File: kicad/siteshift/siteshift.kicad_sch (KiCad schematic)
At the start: 47 parts, among them SW1 Reset, U1 DRV8873HPWPRQ1, U2 Pico, U3 L7805, U4 ULN2004A

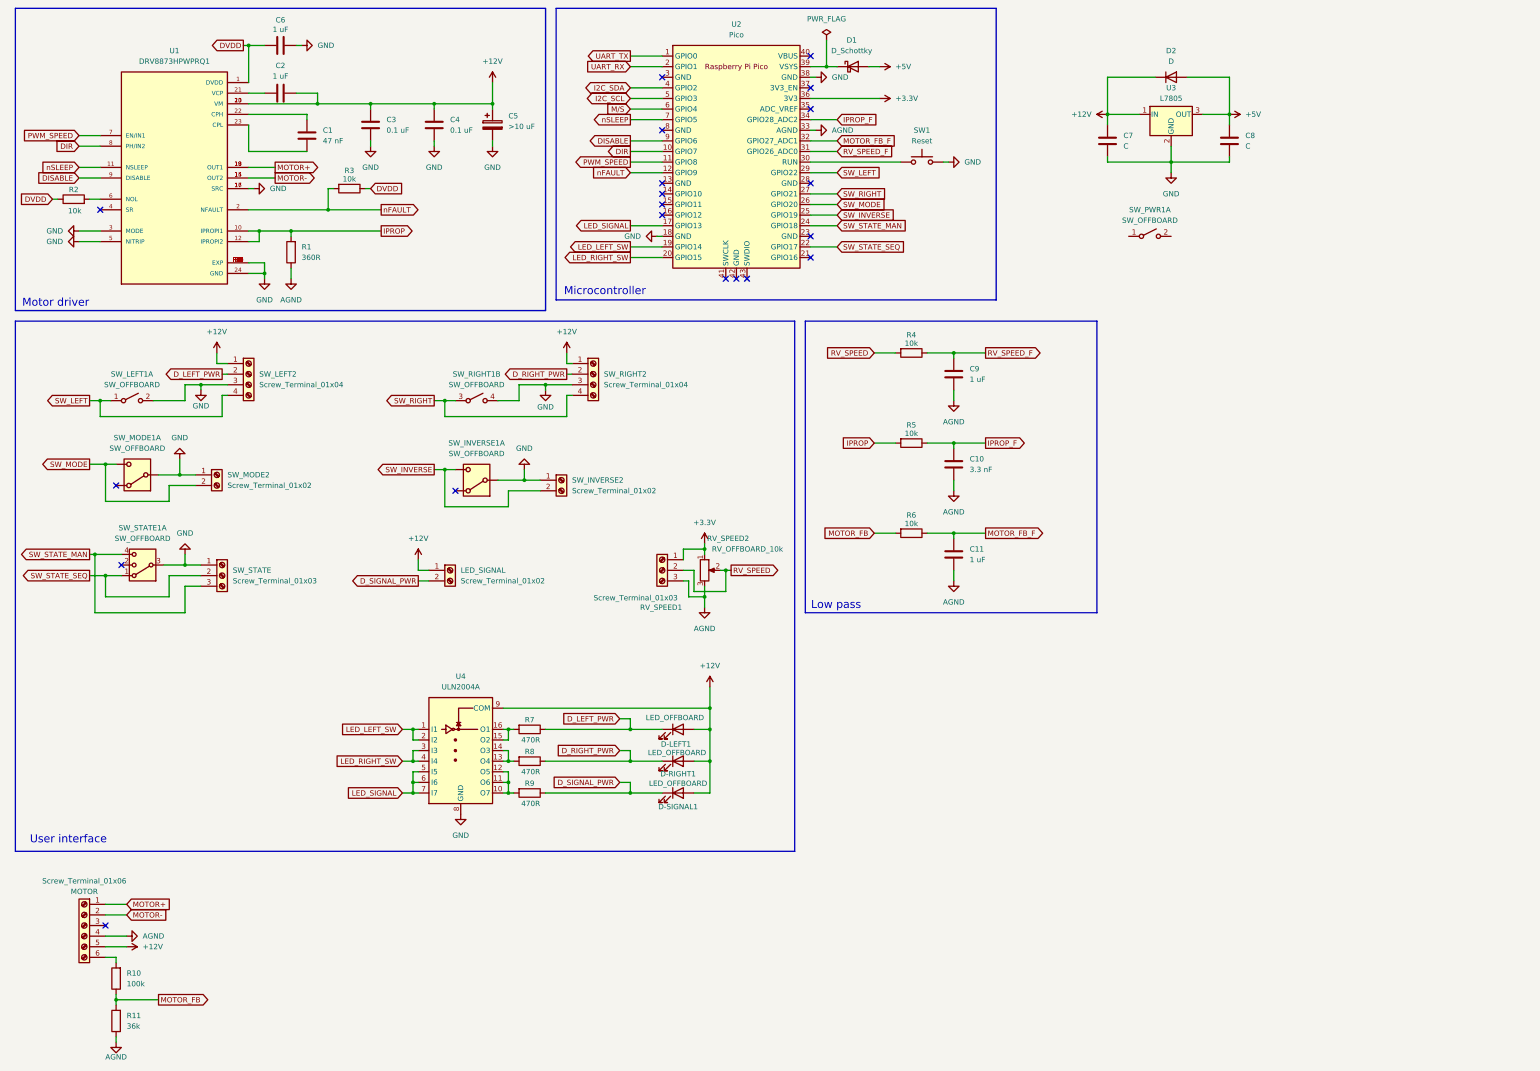
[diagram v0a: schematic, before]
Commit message: Wire power distribution
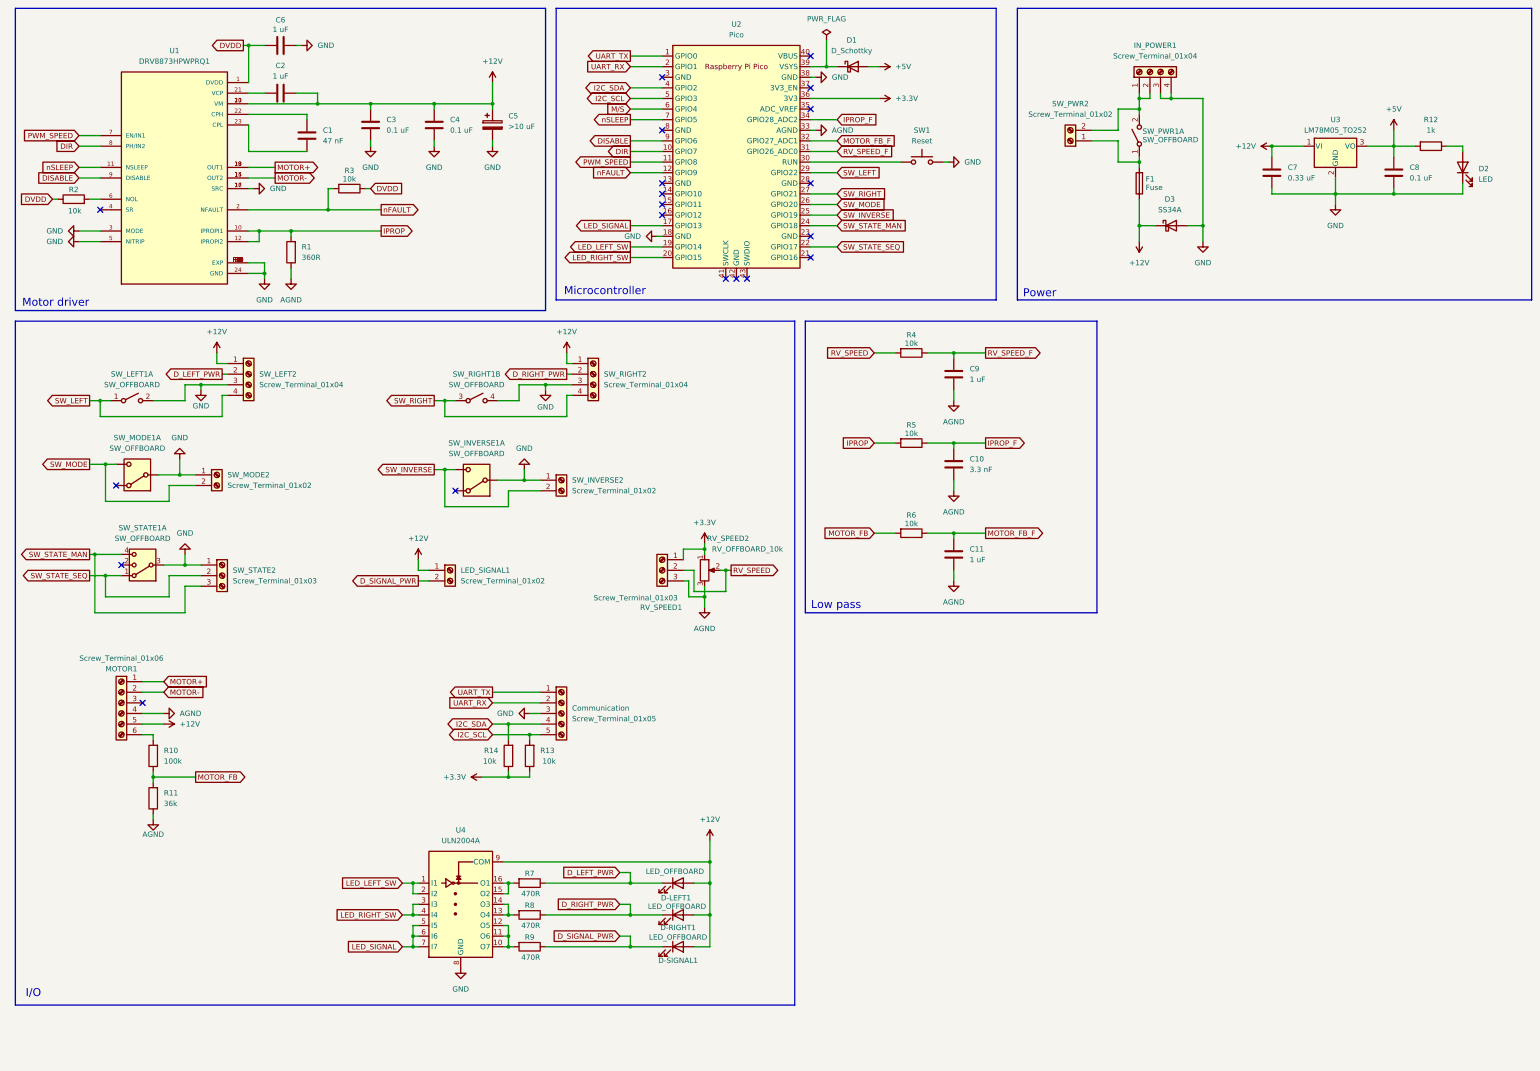
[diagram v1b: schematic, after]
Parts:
- removed D2: D, Diode_SMD:D_1206_3216Metric_Pad1.42x1.75mm_HandSolder, symbol Device:D
- removed U3: L7805, Package_TO_SOT_THT:TO-220-3_Vertical, symbol Regulator_Linear:L7805
- added Communication: Screw_Terminal_01x05, symbol Connector:Screw_Terminal_01x05
- added D2: LED, Diode_SMD:D_1206_3216Metric_Pad1.42x1.75mm_HandSolder, symbol Device:LED
- added D3: SS34A, Diode_SMD:D_SMA_Handsoldering, symbol Device:D_Schottky
- added F1: Fuse, symbol Device:Fuse
- added IN_POWER1: Screw_Terminal_01x04, symbol Connector:Screw_Terminal_01x04
- added R12: 1k, Resistor_SMD:R_1206_3216Metric_Pad1.30x1.75mm_HandSolder, symbol Device:R
- added R13, R14: 10k, symbol Device:R
- added SW_PWR2: Screw_Terminal_01x02, symbol Connector:Screw_Terminal_01x02
- added U3: LM78M05_TO252, Package_TO_SOT_SMD:TO-252-2, symbol Regulator_Linear:LM78M05_TO252
- C7: value C -> 0.33 uF
- C8: value C -> 0.1 uF
- renumbered LED_SIGNAL to LED_SIGNAL1, MOTOR to MOTOR1, SW_STATE to SW_STATE2
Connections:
- net +12V: now also D3.1 (K), F1.1, U3.1 (VI)
- net +3.3V: now also R13.1, R14.1
- net +5V: now also R12.2, U3.3 (VO)
- net GND: now also Communication.3 (Pin_3), D2.1 (K), D3.2 (A), IN_POWER1.3 (Pin_3), IN_POWER1.4 (Pin_4), U3.2 (GND)
- net I2C_SCL: now also Communication.5 (Pin_5), R13.2
- net I2C_SDA: now also Communication.4 (Pin_4), R14.2
- net UART_RX: now also Communication.2 (Pin_2)
- net UART_TX: now also Communication.1 (Pin_1)
- net at SW_PWR1.1 (A): now also F1.2, SW_PWR2.1 (Pin_1)
- net at SW_PWR1.2 (B): now also IN_POWER1.1 (Pin_1), IN_POWER1.2 (Pin_2), SW_PWR2.2 (Pin_2)
- new net: D2.2 (A), R12.1
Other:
- note added: "I/O"
- note added: "Power"
- note removed: "User interface"
- moved on the sheet: C7, C8, D-LEFT1, D-RIGHT1, D-SIGNAL1, MOTOR1, R10, R11, R7, R8, R9, SW_PWR1A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

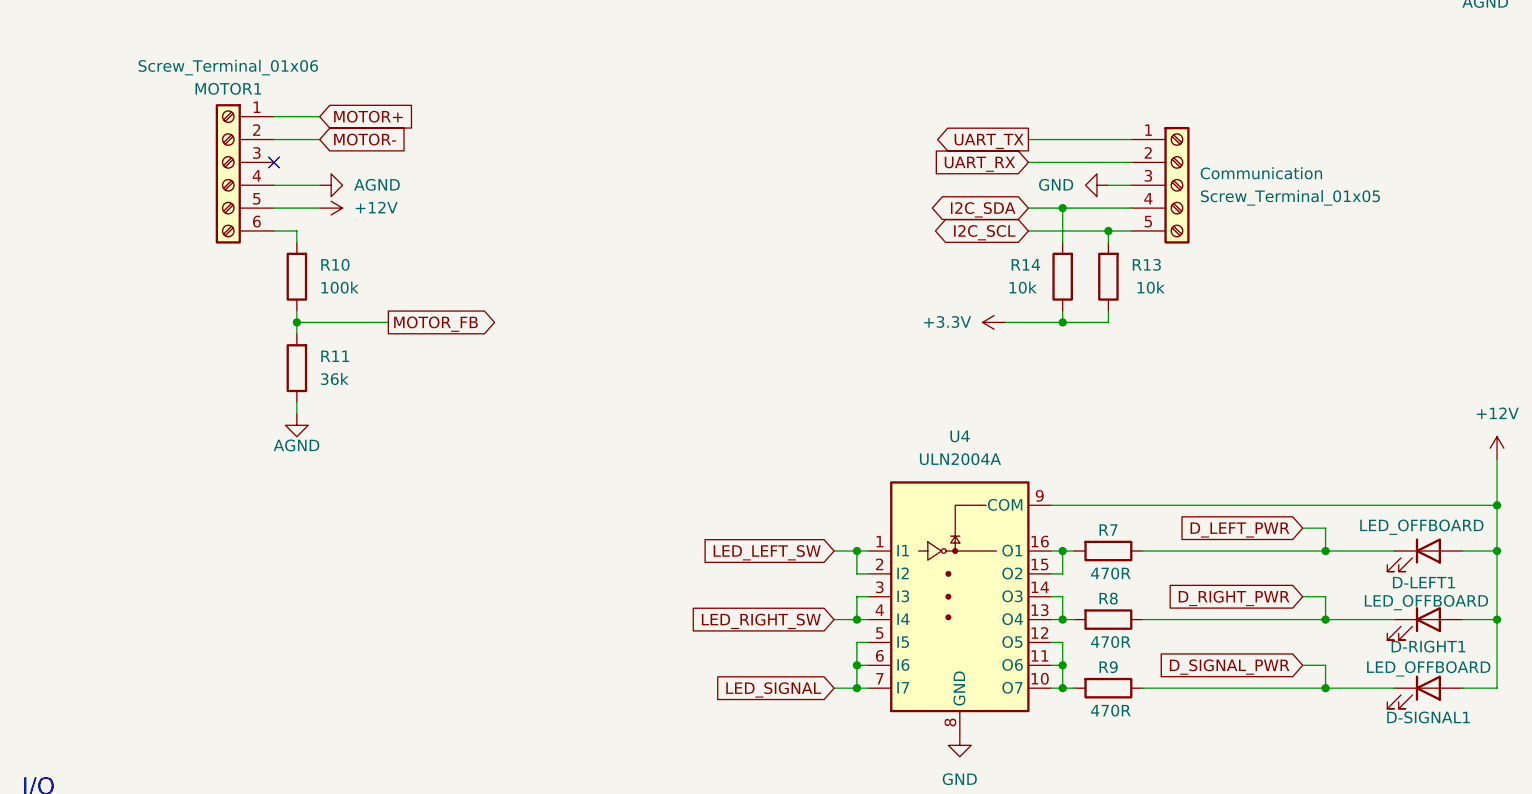
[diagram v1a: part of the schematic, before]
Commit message: Assign footprints
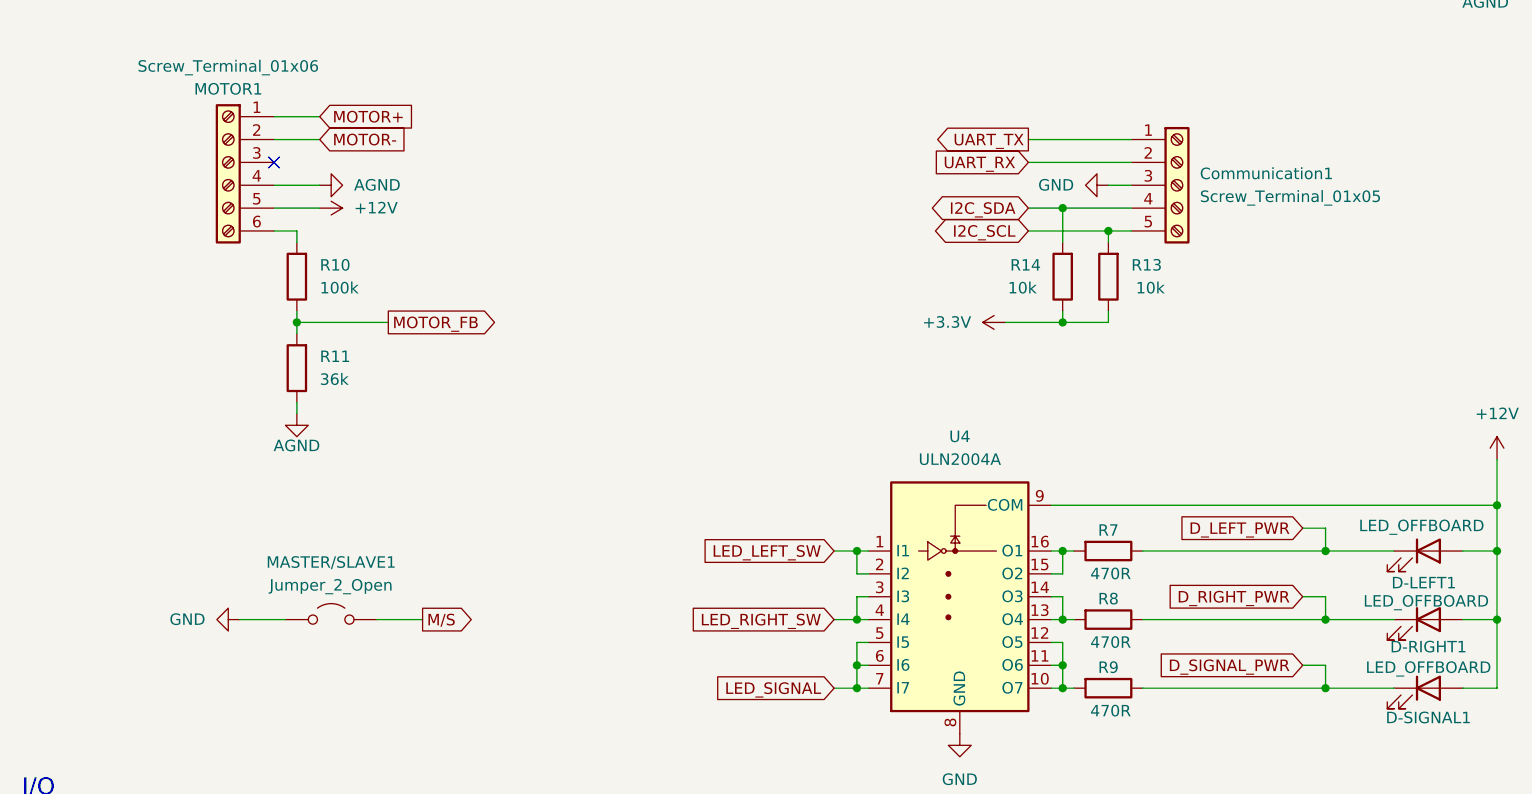
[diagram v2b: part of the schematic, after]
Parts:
- added MASTER/SLAVE1: Jumper_2_Open, Connector_PinHeader_2.54mm:PinHeader_1x03_P2.54mm_Vertical, symbol Jumper:Jumper_2_Open
- C1, C10, C11, C2, C3, C4, C6, C9: footprint (none) -> Capacitor_SMD:C_1206_3216Metric_Pad1.33x1.80mm_HandSolder
- C5: footprint (none) -> Capacitor_Tantalum_SMD:CP_EIA-6032-20_AVX-F_Pad2.25x2.35mm_HandSolder
- Communication1: renamed from Communication; footprint (none) -> TerminalBlock_MetzConnect:TerminalBlock_MetzConnect_Type101_RT01605HBWC_1x05_P5.08mm_Horizontal
- D3: footprint Diode_SMD:D_SMA_Handsoldering -> Diode_SMD:D_SMB-SMC_Universal_Handsoldering
- F1: footprint (none) -> Fuse:Fuse_Blade_ATO_directSolder
- IN_POWER1, SW_LEFT2, SW_RIGHT2: footprint (none) -> TerminalBlock_MetzConnect:TerminalBlock_MetzConnect_Type101_RT01604HBWC_1x04_P5.08mm_Horizontal
- LED_SIGNAL1, SW_INVERSE2, SW_MODE2, SW_PWR2: footprint (none) -> TerminalBlock_MetzConnect:TerminalBlock_MetzConnect_Type101_RT01602HBWC_1x02_P5.08mm_Horizontal
- MOTOR1: footprint (none) -> TerminalBlock_MetzConnect:TerminalBlock_MetzConnect_Type101_RT01606HBWC_1x06_P5.08mm_Horizontal
- R1, R10, R11, R13, R14, R2, R3, R4, R5, R6, R7, R8, R9: footprint (none) -> Resistor_SMD:R_1206_3216Metric_Pad1.30x1.75mm_HandSolder
- RV_SPEED1, SW_STATE2: footprint (none) -> TerminalBlock_MetzConnect:TerminalBlock_MetzConnect_Type101_RT01603HBWC_1x03_P5.08mm_Horizontal
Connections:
- net GND: now also MASTER/SLAVE1.1 (A)
- net M/S: now also MASTER/SLAVE1.2 (B)

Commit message: first pcb design
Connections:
- net GND: now also U2.3 (GND); no longer U2.18 (GND)

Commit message: PCB design update
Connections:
- net IPROP_F: now also U2.31 (GPIO26_ADC0); no longer U2.34 (GPIO28_ADC2)
- net RV_SPEED_F: now also U2.34 (GPIO28_ADC2); no longer U2.31 (GPIO26_ADC0)
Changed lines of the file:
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@@
+		)
+	)
+	(global_label "RV_SPEED_F"
+		(shape input)
+		(at 210.82 40.64 0)
+		(fields_autoplaced yes)
+		(effects
+			(font
+				(size 1.27 1.27)
+			)
+			(justify left)
+		)
+		(property "Intersheetrefs" "${INTERSHEET_REFS}"
+			(at 225.2351 40.64 0)
+			(effects
+				(font
+					(size 1.27 1.27)
+				)
+				(justify left)
+				(hide yes)
+			)
 		)
 	)
@@
 		)
 	)
+	(global_label "PWM_SPEED"
+		(shape output)
+		(at 161.29 50.8 180)
+		(fields_autoplaced yes)
+		(effects
+			(font
+				(size 1.27 1.27)
+			)
+			(justify right)
+		)
+		(property "Intersheetrefs" "${INTERSHEET_REFS}"
+			(at 147.1169 50.8 0)
+			(effects
+				(font
+					(size 1.27 1.27)
+				)
+				(justify right)
+				(hide yes)
+			)
+		)
+	)
+	(global_label "LED_RIGHT_SW"
+		(shape output)
+		(at 161.29 73.66 180)
+		(fields_autoplaced yes)
+		(effects
+			(font
+				(size 1.27 1.27)
+			)
+			(justify right)
+		)
+		(property "Intersheetrefs" "${INTERSHEET_REFS}"
+			(at 144.8187 73.66 0)
+			(effects
+				(font
+					(size 1.27 1.27)
+				)
+				(justify right)
+				(hide yes)
+			)
+		)
+	)
+	(global_label "MOTOR_FB"
+		(shape output)
+		(at 57.15 198.12 0)
+		(fields_autoplaced yes)
+		(effects
+			(font
+				(size 1.27 1.27)
+			)
+			(justify left)
+		)
+		(property "Intersheetrefs" "${INTERSHEET_REFS}"
+			(at 69.8114 198.12 0)
+			(effects
+				(font
+					(size 1.27 1.27)
+				)
+				(justify left)
+				(hide yes)
+			)
+		)
+	)
 	(global_label "IPROP_F"
 		(shape input)
-		(at 210.82 40.64 0)
-		(fields_autoplaced yes)
-		(effects
-			(font
-				(size 1.27 1.27)
-			)
-			(justify left)
-		)
-		(property "Intersheetrefs" "${INTERSHEET_REFS}"
-			(at 221.6067 40.64 0)
+		(at 210.82 48.26 0)
+		(fields_autoplaced yes)
+		(effects
+			(font
+				(size 1.27 1.27)
+			)
+			(justify left)
+		)
+		(property "Intersheetrefs" "${INTERSHEET_REFS}"
+			(at 221.6067 48.26 0)
 			(effects
 				(font
@@
 	)
 	(global_label "PWM_SPEED"
-		(shape output)
-		(at 161.29 50.8 180)
-		(fields_autoplaced yes)
-		(effects
-			(font
-				(size 1.27 1.27)
-			)
-			(justify right)
-		)
-		(property "Intersheetrefs" "${INTERSHEET_REFS}"
-			(at 147.1169 50.8 0)
-			(effects
-				(font
-					(size 1.27 1.27)
-				)
-				(justify right)
-				(hide yes)
-			)
-		)
-	)
-	(global_label "LED_RIGHT_SW"
-		(shape output)
-		(at 161.29 73.66 180)
-		(fields_autoplaced yes)
-		(effects
-			(font
-				(size 1.27 1.27)
-			)
-			(justify right)
-		)
-		(property "Intersheetrefs" "${INTERSHEET_REFS}"
-			(at 144.8187 73.66 0)
-			(effects
-				(font
-					(size 1.27 1.27)
-				)
-				(justify right)
-				(hide yes)
-			)
-		)
-	)
-	(global_label "MOTOR_FB"
-		(shape output)
-		(at 57.15 198.12 0)
-		(fields_autoplaced yes)
-		(effects
-			(font
-				(size 1.27 1.27)
-			)
-			(justify left)
-		)
-		(property "Intersheetrefs" "${INTERSHEET_REFS}"
-			(at 69.8114 198.12 0)
-			(effects
-				(font
-					(size 1.27 1.27)
-				)
-				(justify left)
-				(hide yes)
-			)
-		)
-	)
-	(global_label "PWM_SPEED"
 		(shape input)
 		(at 29.21 44.45 180)
@@
 				(hide yes)
 			)
-		)
-	)
-	(global_label "RV_SPEED_F"
-		(shape input)
-		(at 210.82 48.26 0)
-		(fields_autoplaced yes)
-		(effects
-			(font
-				(size 1.27 1.27)
-			)
-			(justify left)
-		)
-		(property "Intersheetrefs" "${INTERSHEET_REFS}"
-			(at 225.2351 48.26 0)
-			(effects
-				(font
-					(size 1.27 1.27)
-				)
-				(justify left)
-				(hide yes)
-			)

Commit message: First code setup
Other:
- moved on the sheet: C2
